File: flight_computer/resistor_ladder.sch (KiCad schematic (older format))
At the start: 26 parts, among them U10 ADG841YKSZ-500RL7, U11 ADG841YKSZ-500RL7, U12 ADG841YKSZ-500RL7, U13 ADG841YKSZ-500RL7, U6 ADG841YKSZ-500RL7, U7 ADG841YKSZ-500RL7, U8 ADG841YKSZ-500RL7, U9 ADG841YKSZ-500RL7

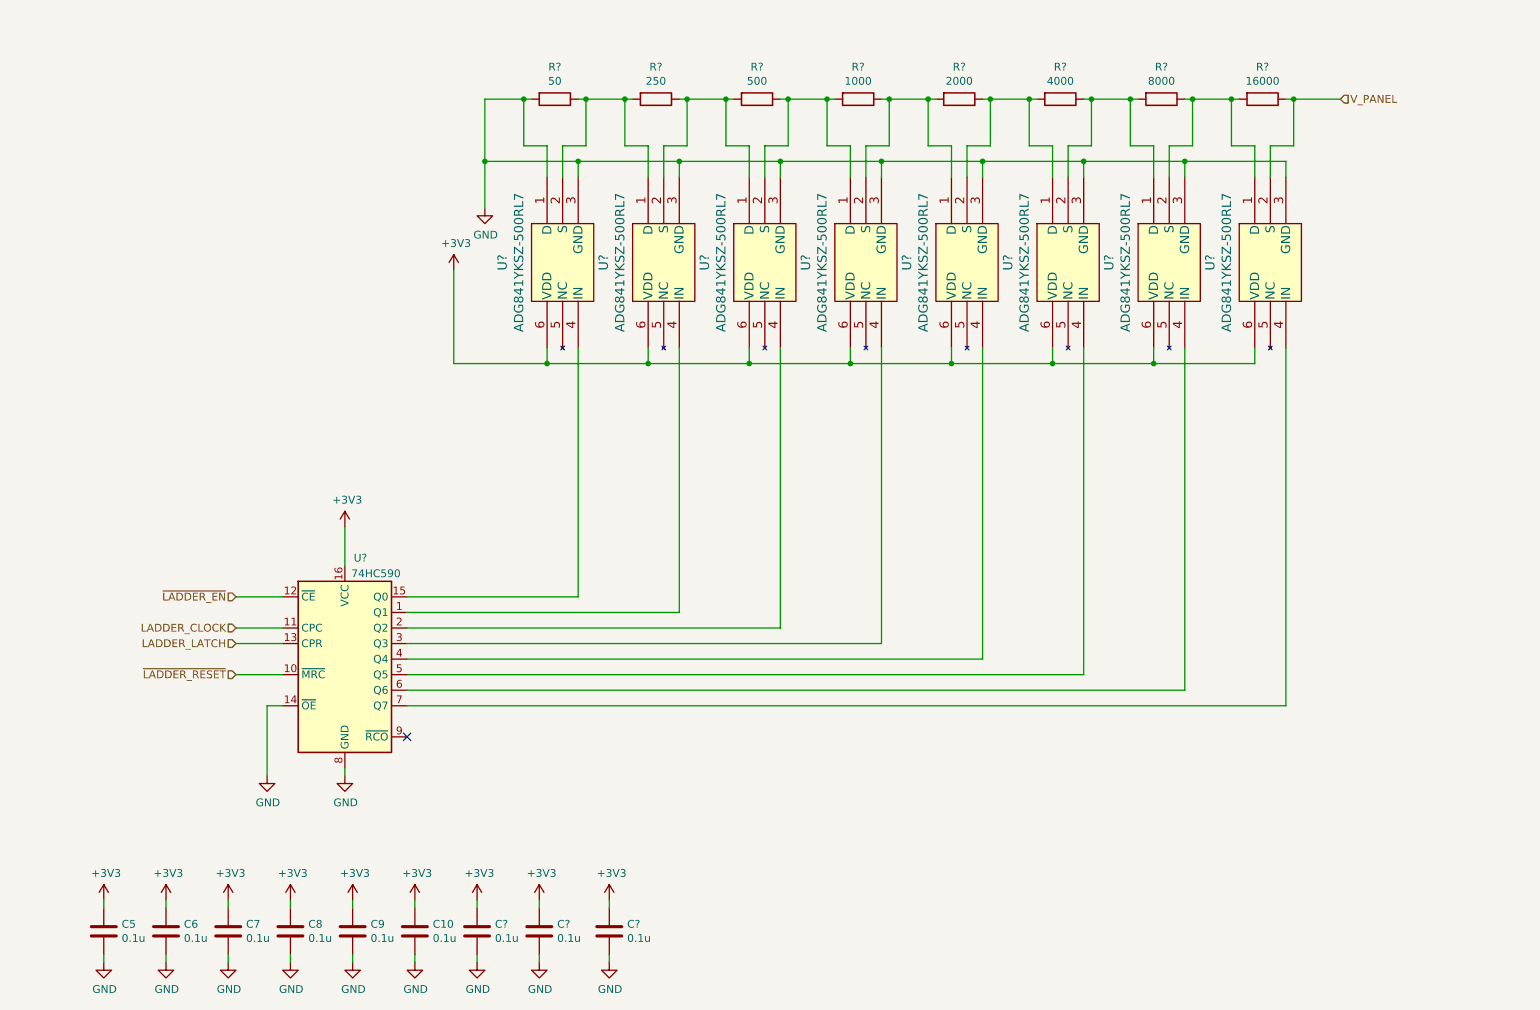
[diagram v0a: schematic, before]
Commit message: Working on flight computer
- Update resistor ladder curve tracer silkscreen, schematic, and layout
- Flight computer schematic drafted for MSP430 circuits, updated curve tracer, perovskite switching network.
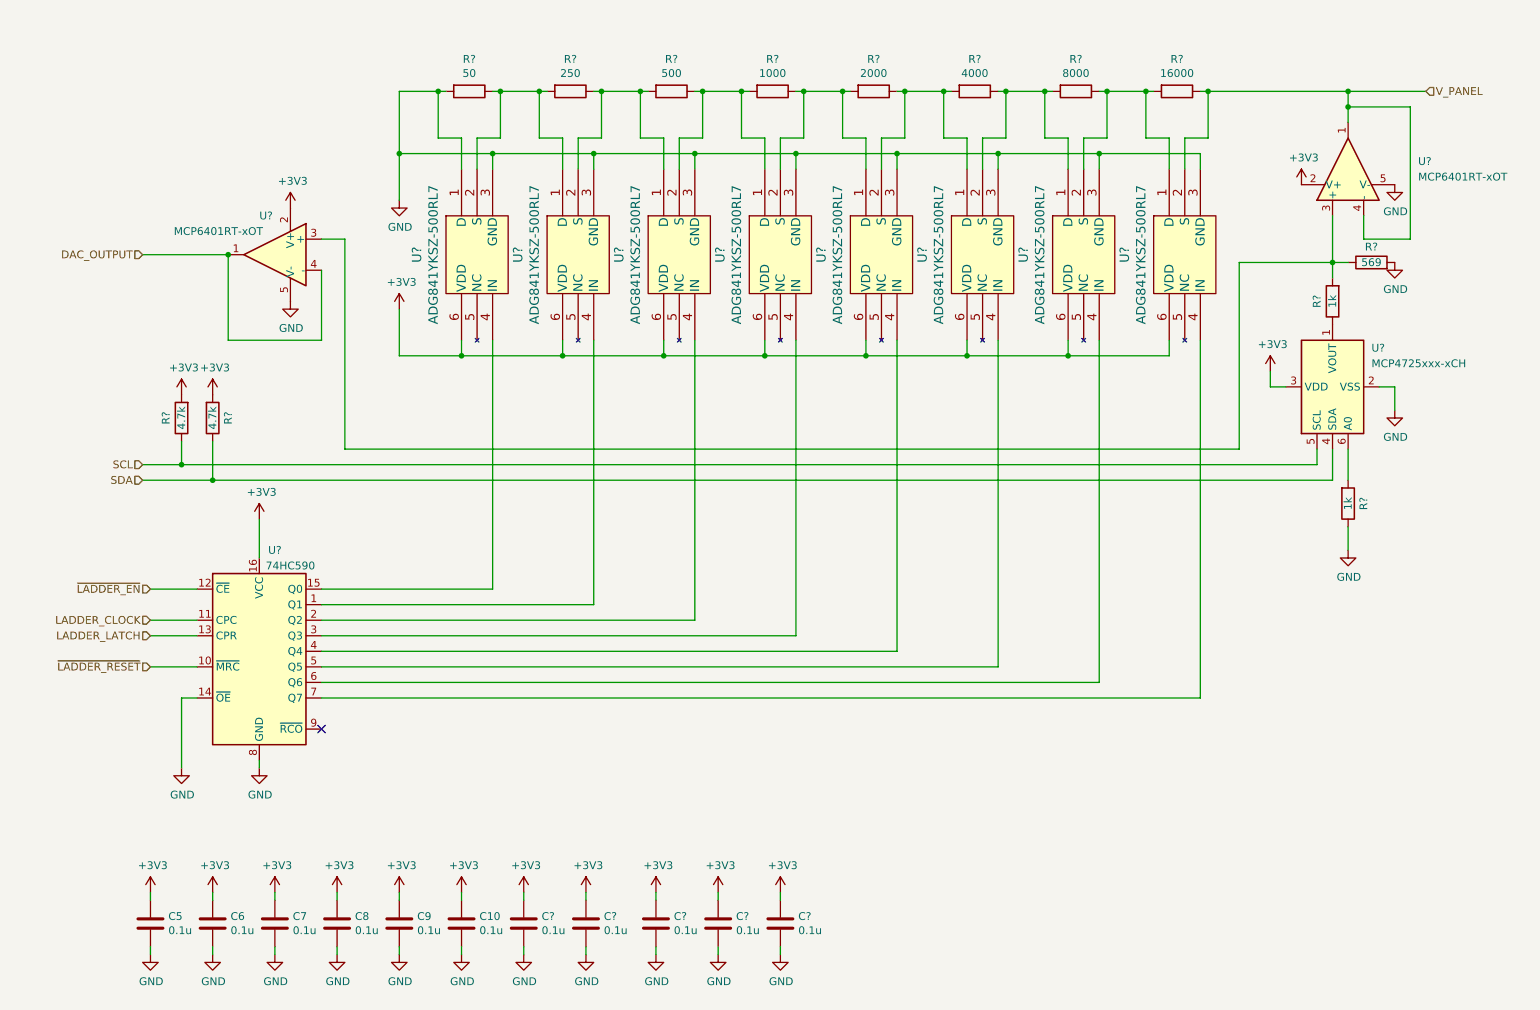
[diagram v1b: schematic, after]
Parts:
- added C? (x2): 0.1u, Capacitor_SMD:C_0603_1608Metric, symbol Device:C
- added R? (x2): 4.7k, Resistor_SMD:R_0603_1608Metric, symbol Device:R
- added R? (x2): 1k, Resistor_SMD:R_0603_1608Metric, symbol Device:R
- added R?: 569, Resistor_SMD:R_0603_1608Metric, symbol Device:R
- added U?: MCP4725xxx-xCH, Package_TO_SOT_SMD:SOT-23-6, symbol Analog_DAC:MCP4725xxx-xCH
- added U? (x2): MCP6401RT-xOT, Package_TO_SOT_SMD:SOT-23-5, symbol Amplifier_Operational:MCP6401RT-xOT
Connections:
- net +3V3: now also C?.1, C?.1, R?.2, R?.2, U?.2 (V+), U?.2 (V+), U?.3 (VDD)
- net GND: now also C?.2, C?.2, R?.1, R?.2, U?.2 (VSS), U?.5 (V-), U?.5 (V-)
- net V_PANEL: now also U?.1, U?.4 (-)
- new net: R?.1, U?.1 (VOUT)
- new net: R?.2, U?.6 (A0)
- new net: R?.1, R?.2, U?.3 (+), U?.3 (+)
- new net DAC_OUTPUT: U?.1, U?.4 (-)
- new net SCL: R?.1, U?.5 (SCL)
- new net SDA: R?.1, U?.4 (SDA)
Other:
- moved on the sheet: C10, C5, C6, C7, C8, C9, C?, R?, U?

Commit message: Update flight computer schematic
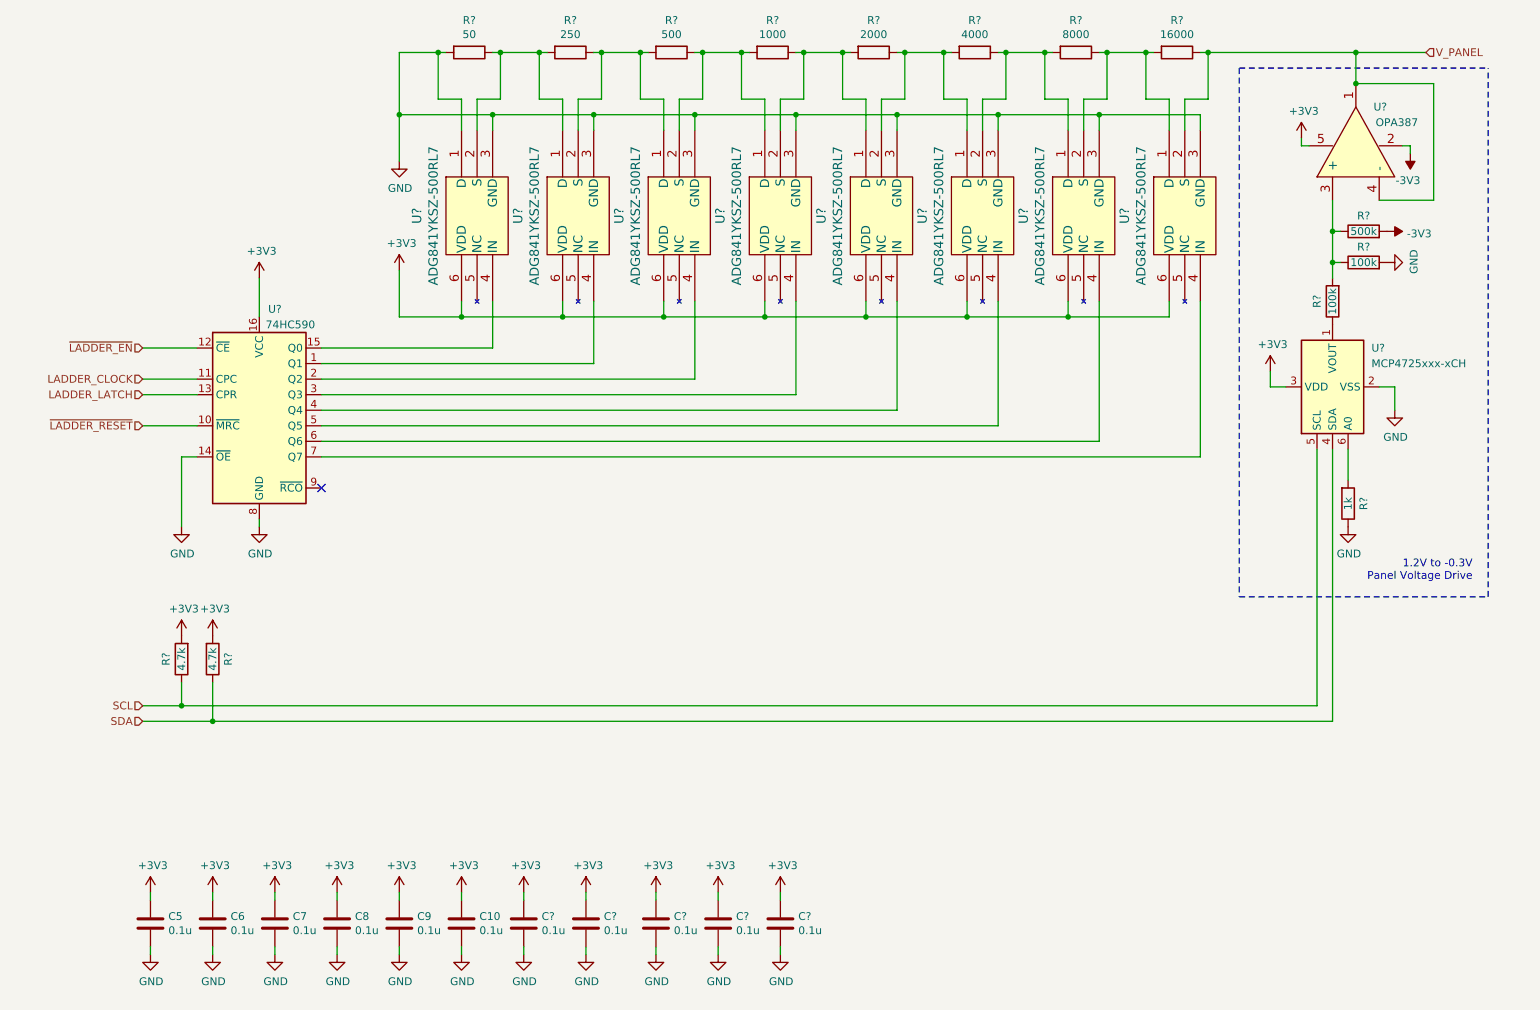
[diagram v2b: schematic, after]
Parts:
- removed U? (x2): MCP6401RT-xOT, Package_TO_SOT_SMD:SOT-23-5, symbol Amplifier_Operational:MCP6401RT-xOT
- added R?: 500k, Resistor_SMD:R_0603_1608Metric, symbol Device:R
- added U?: OPA387, symbol OPA387:OPA387
- R?: value 1k -> 100k
- R?: value 569 -> 100k
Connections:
- net +3V3: now also U?.5
- net V_PANEL: now also U?.1, U?.4 (-)
- net at R?.1, R?.2: now also R?.1, U?.3 (+)
- new net -3V3: R?.2, U?.2
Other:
- note added: "1.2V to -0.3V\nPanel Voltage Drive"
- moved on the sheet: R?, U?

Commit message: Annotating schematic with references and footprints
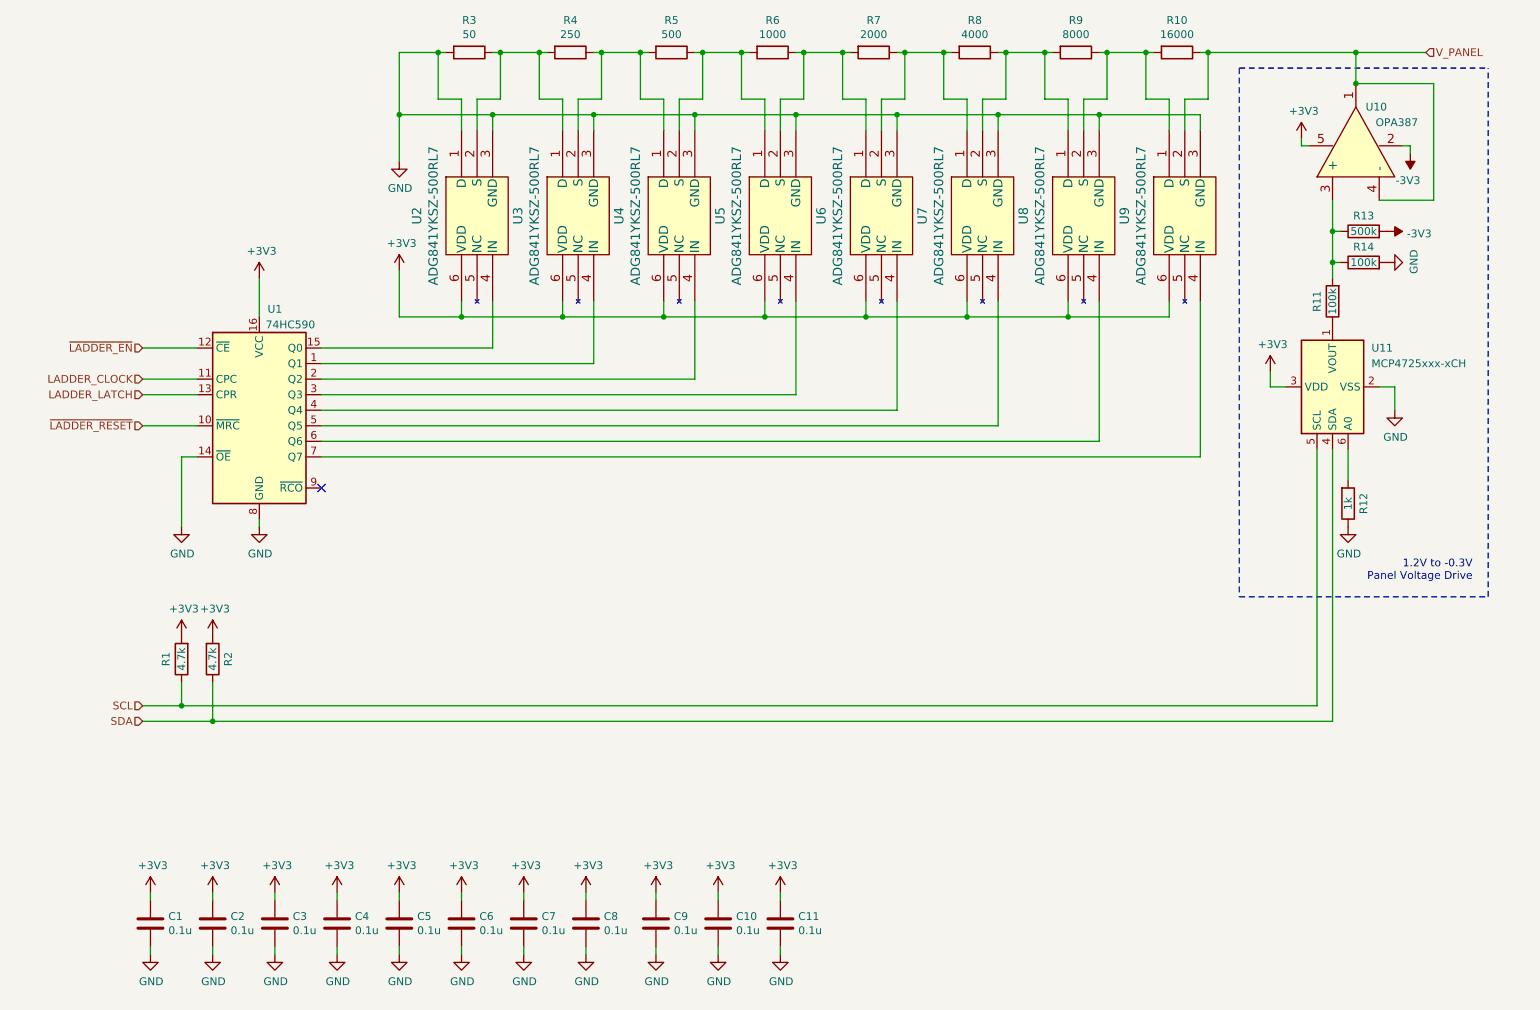
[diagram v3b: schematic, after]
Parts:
- gave numbers to parts that had none: 22

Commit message: Continuing layout
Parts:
- removed C9: 0.1u, Capacitor_SMD:C_0603_1608Metric, symbol Device:C
- removed U10: OPA387, symbol OPA387:OPA387
- added U10: OPA2387, Package_SON:WSON-8-1EP_2x2mm_P0.5mm_EP0.9x1.6mm, symbol OPA2387:OPA2387
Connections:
- net +3V3: now also U10.8
- net -3V3: now also U10.4
- net V_PANEL: now also U10.1, U10.2 (-)
- net at R11.2, R13.1, R14.1: now also U10.3 (+)
